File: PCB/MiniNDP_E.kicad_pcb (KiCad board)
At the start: 2 copper layers, 60 x 34 mm, 23 parts, among them J1 Conn_02x20_Odd_Even, U1 HC161, U2 HC161, U3 HC161, U4 HC138, U5 HC574, U6 AS6C4008, U7 1G32, U8 1G79

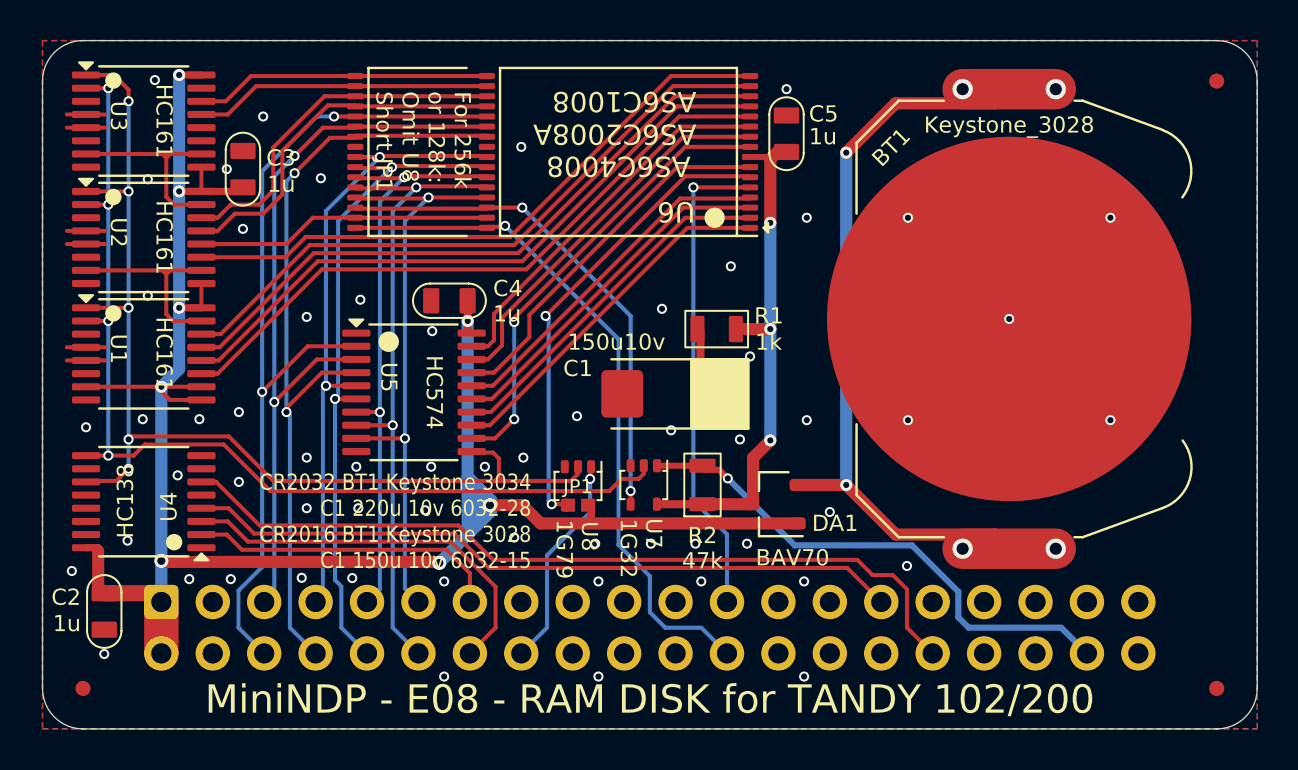
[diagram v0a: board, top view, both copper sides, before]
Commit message: rename 512_F to EZ512
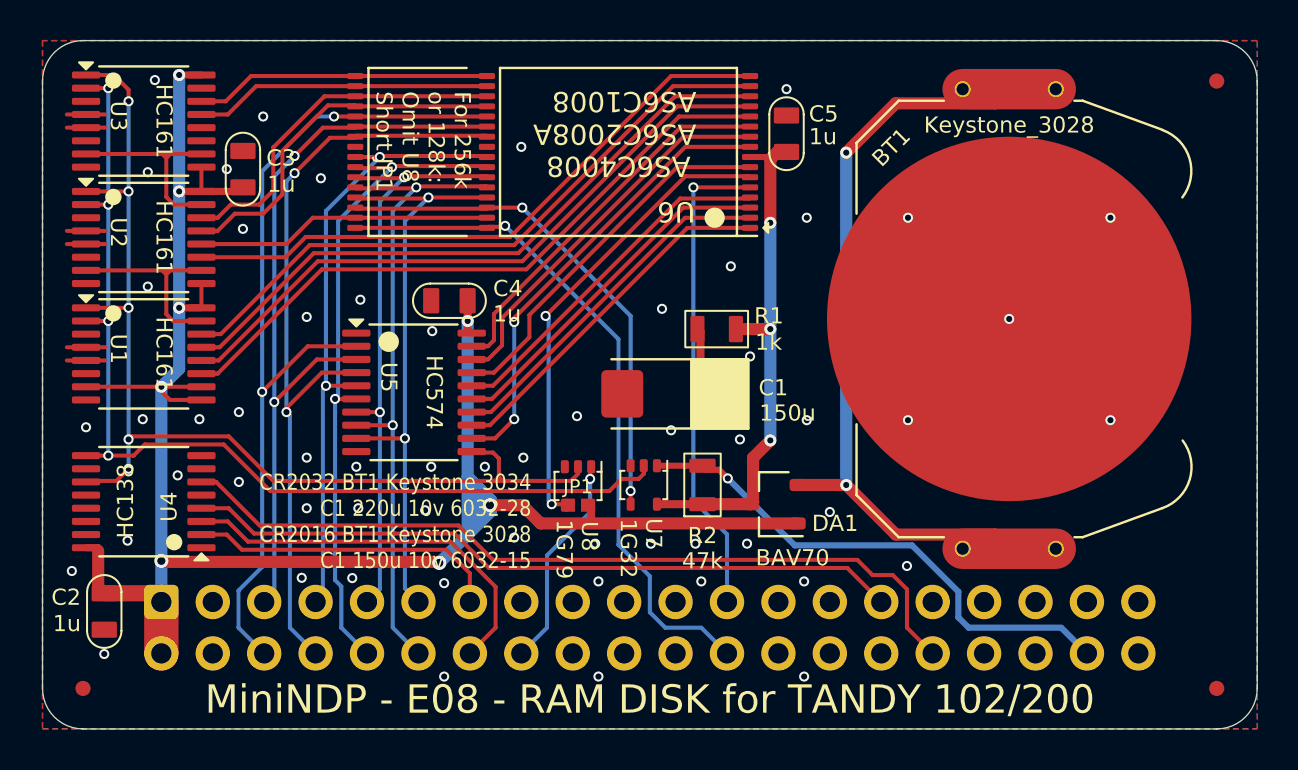
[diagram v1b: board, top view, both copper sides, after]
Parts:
- added REF**: pth_nail, 000_LOCAL:pth_nail, F.Cu at (167.4, 88.4)
- added REF**: pth_nail, 000_LOCAL:pth_nail, F.Cu at (172.0, 111.1)
- added REF**: pth_nail, 000_LOCAL:pth_nail, F.Cu at (172.0, 88.4)
- added REF**: pth_nail, 000_LOCAL:pth_nail, F.Cu at (167.4, 111.1)
- C1: value 150u10v -> 150u
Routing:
- net GND: vias 60 -> 58
- net +BATT: vias 6 -> 2
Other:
- board text added: "OUT 129,N bank 0 block N OUT 133,N bank 1 block N N=INP(131) read byte OUT 131,N write byte"

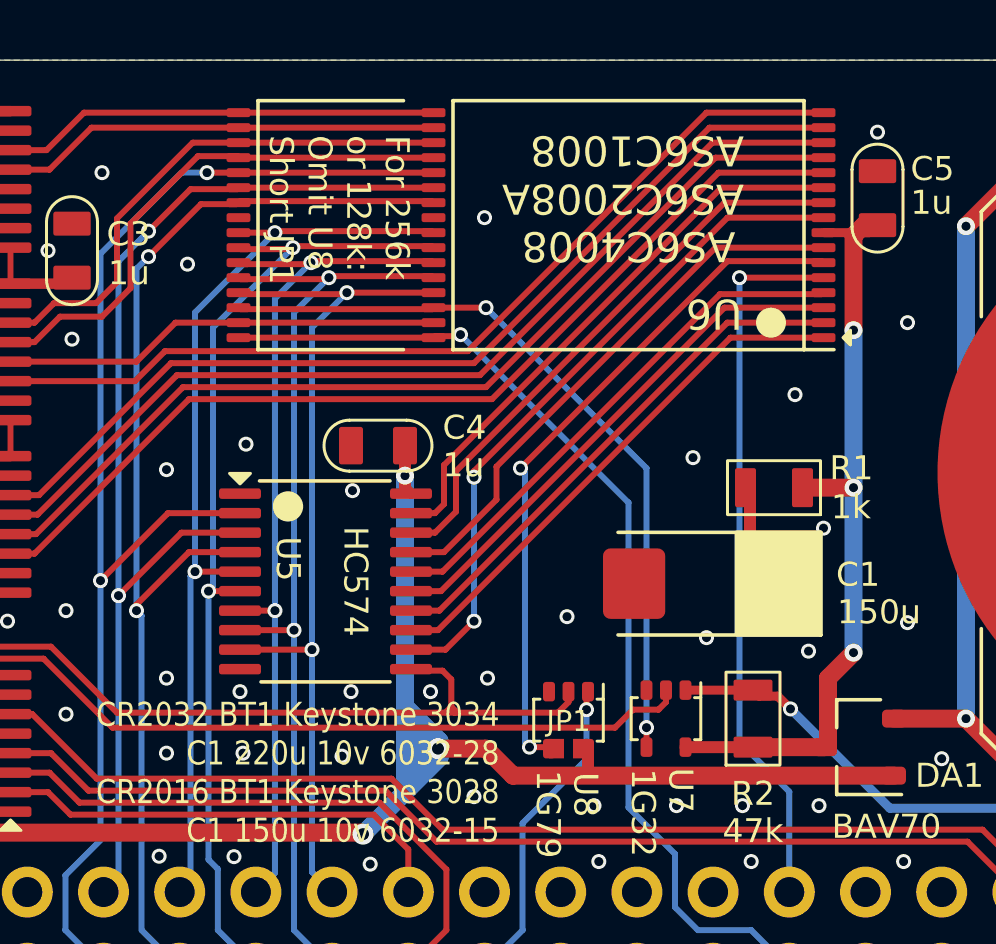
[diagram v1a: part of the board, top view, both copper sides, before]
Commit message: rename 256_F to EZ256
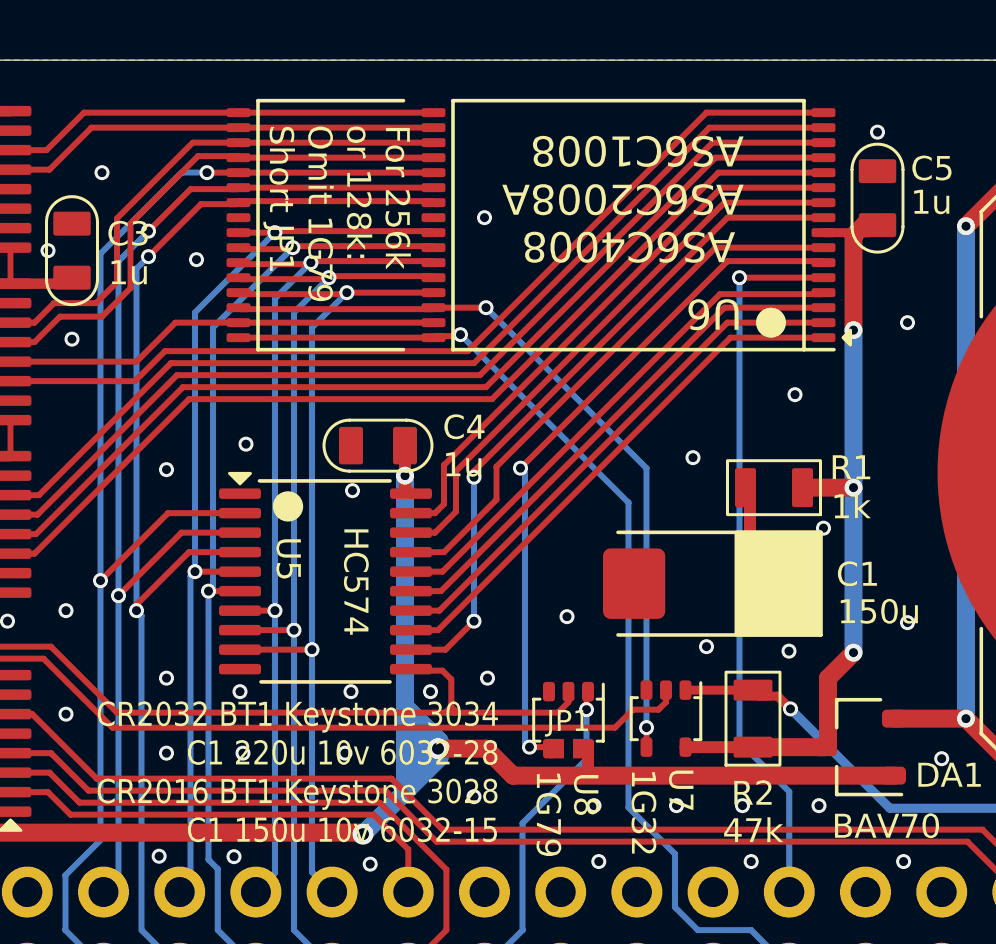
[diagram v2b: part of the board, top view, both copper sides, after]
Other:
- board text added: "For 256k or 128k: Omit 1G79 Short JP1"
- board text added: "bank0-1: P=129,133 block0-255: OUT P,N read byte: N=INP(131) write byte: OUT 131,N"
- board text removed: "For 256k or 128k: Omit U8 Short JP1"
- board text removed: "OUT 129,N bank 0 block N OUT 133,N bank 1 block N N=INP(131) read byte OUT 131,N write byte"
